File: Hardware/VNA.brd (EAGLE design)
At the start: 122 x 96 mm, 502 parts, among them IC1 MIC2253, IC10 MAX2871, IC11 RFSW6042, IC12 RFSW6042, IC13 QPC6324, IC14 RFSA3714, IC15 TRF37A73, IC16 QPC6324, IC17 QPC6324, IC18 QPC6324, IC19 AP2114H, IC2 LM3370SD-4221, IC20 NCP702-3.3, IC21 MAX2871, IC22 LT5560, IC23 THS4521IDGKR, IC24 ADL5801, IC25 NCP702-1.8, IC26 MCP33131D-10-E/MS, IC27 LT5560, IC28 THS4521IDGKR, IC29 ADL5801, IC3 LDL212PU50R, IC30 NCP702-1.8, IC31 MCP33131D-10-E/MS, IC32 THS4521IDGKR, IC33 ADL5801, IC34 NCP702-1.8, IC35 MCP33131D-10-E/MS, IC36 LT5560, IC37 STM32G431CB, IC4 LDL212PU50R, IC5 LDL212PU50R, IC6 LDL212PU50R, IC7 SI5351C, IC8 AP2114H, IC9 NCP702-3.3, J1 DNP, J2 AMPHENOL_132289, J3 AMPHENOL_132289, J4 TYPE-C16P(073), Q1 DSB221SDN/26MHz, T1 B012-617DB-1-63-B331, T2 B012-617DB-1-63-B331, T3 B012-617DB-1-63-B331, U1 W25Q16BVSN, U2 6SLX9TQG144, X1 SMA_CONNECTOR, X2 SMA_CONNECTOR, X3 DNP

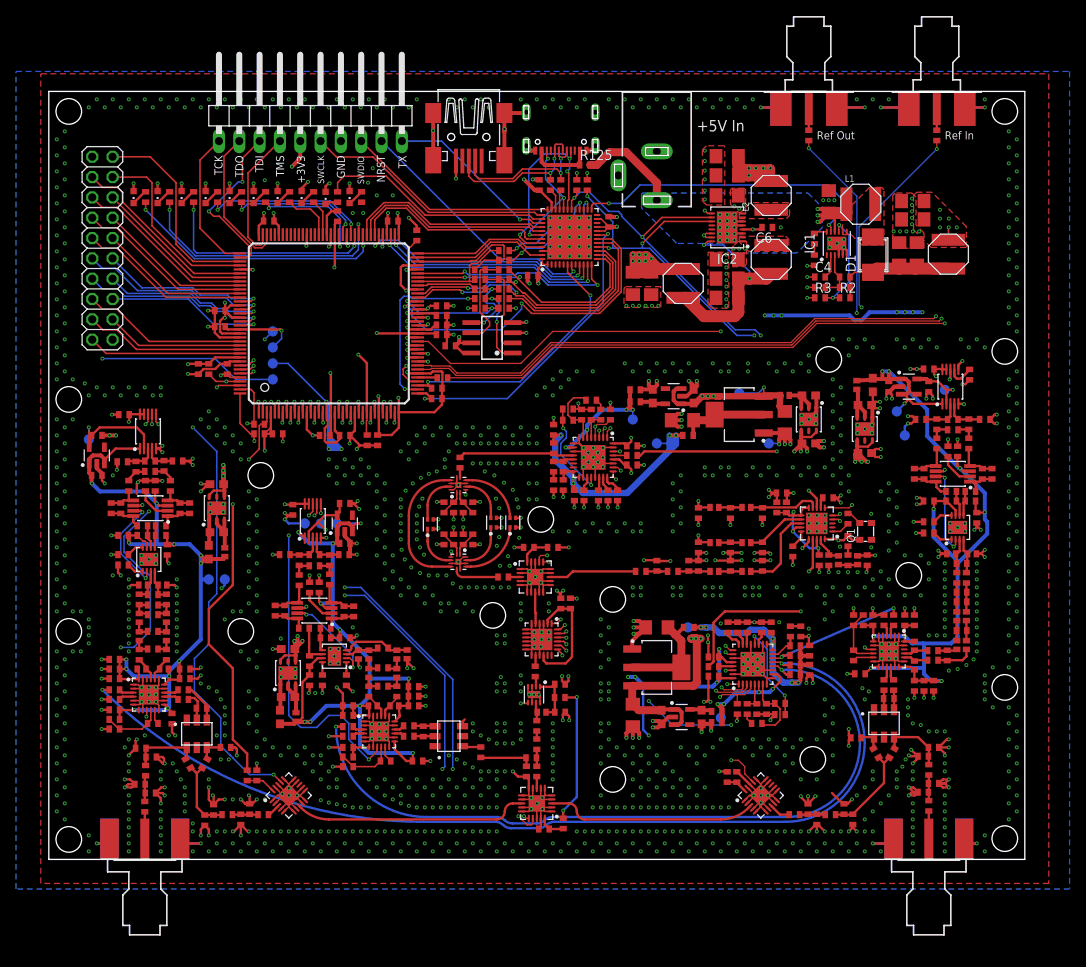
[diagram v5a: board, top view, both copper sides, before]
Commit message: Additional screws
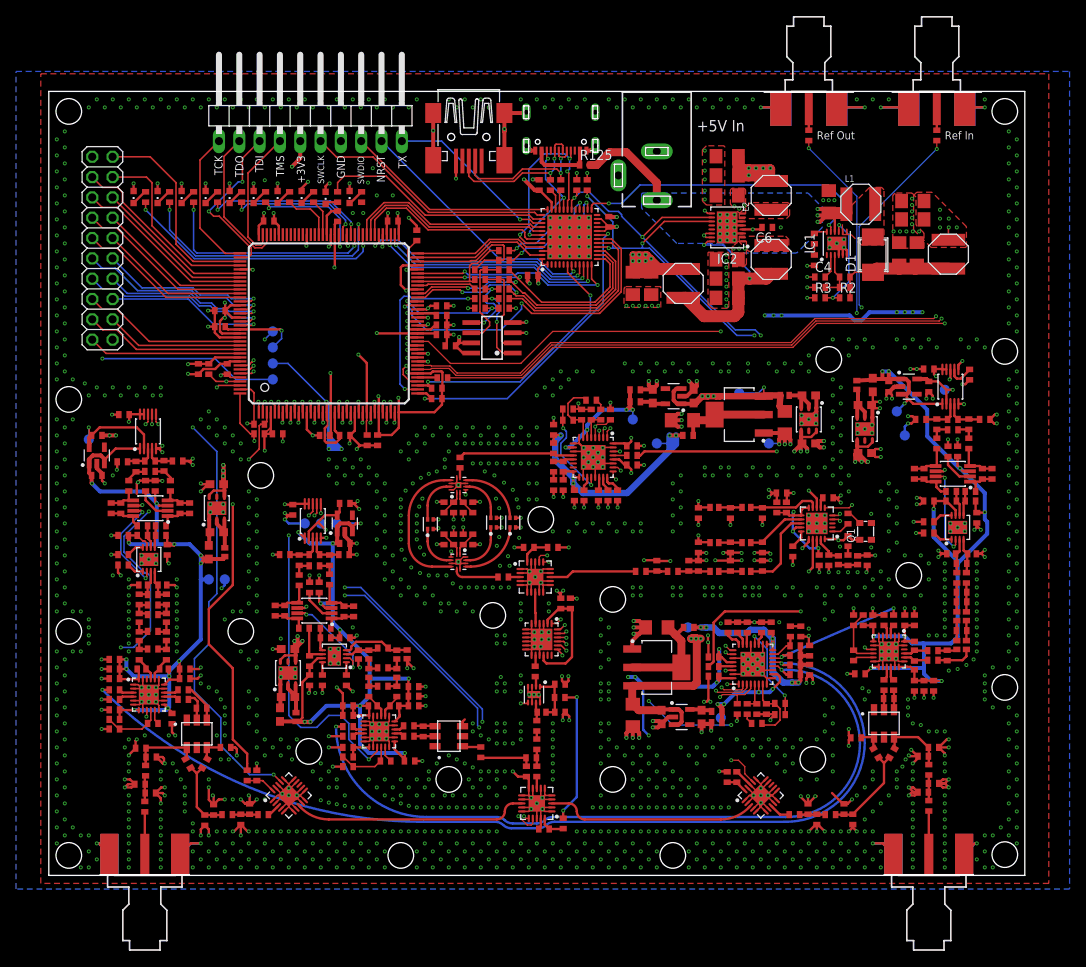
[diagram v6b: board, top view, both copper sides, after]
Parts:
- moved J2 1.90 mm to (12.0, -1.90)
- moved J3 1.90 mm to (110.0, -1.90)
- moved C175 1.00 mm to (45.1, 12.3)
- moved C28 0.30 mm to (28.9, 18.1)
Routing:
- net PORTSWITCH2: track 71.5 -> 69.2 mm
- net PORTSWITCH1: track 70.6 -> 68.3 mm
- net GND: track 729.2 -> 731.5 mm, vias 1584 -> 1681
- net +5V/3: track 106.3 -> 104.3 mm
- net N$6: track 3.38 -> 5.28 mm
- net N$239: track 3.48 -> 5.38 mm
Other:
- board size 122 x 96 mm -> 122 x 98 mm

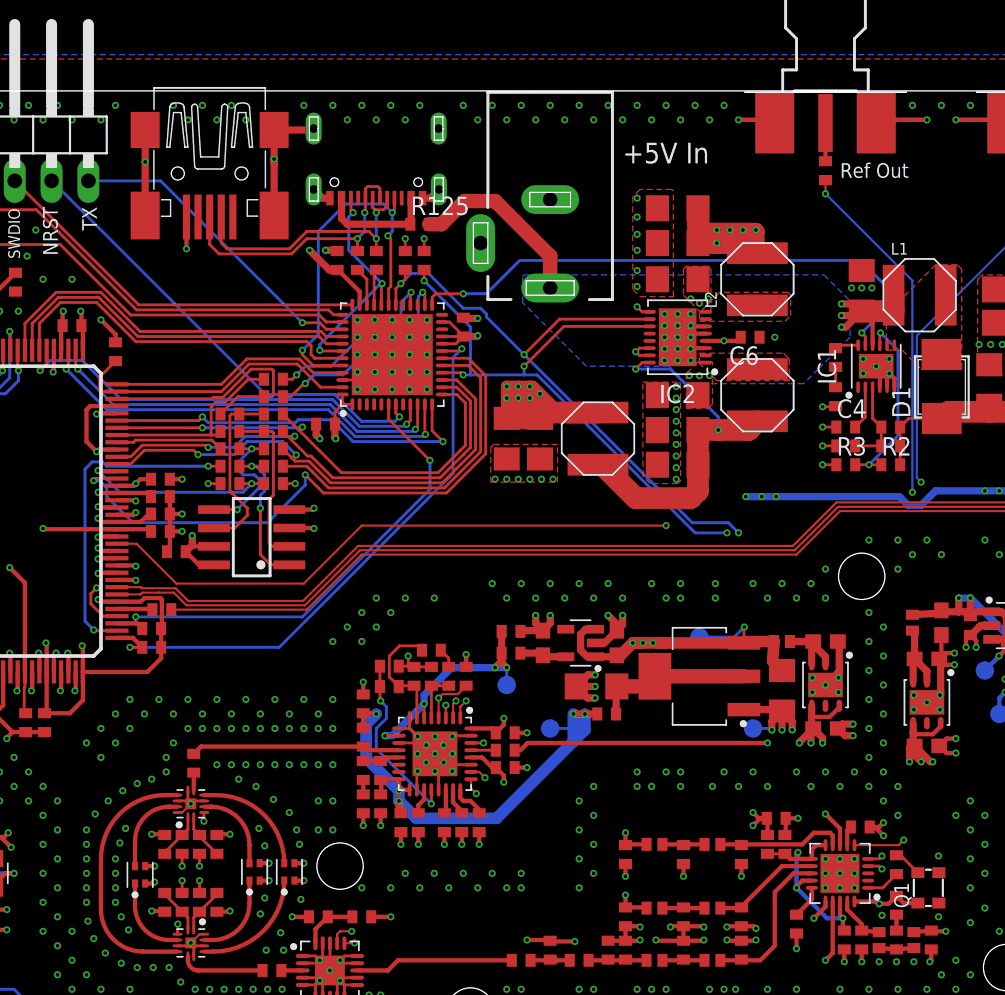
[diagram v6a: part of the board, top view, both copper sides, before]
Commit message: DC jack with power priority over USB
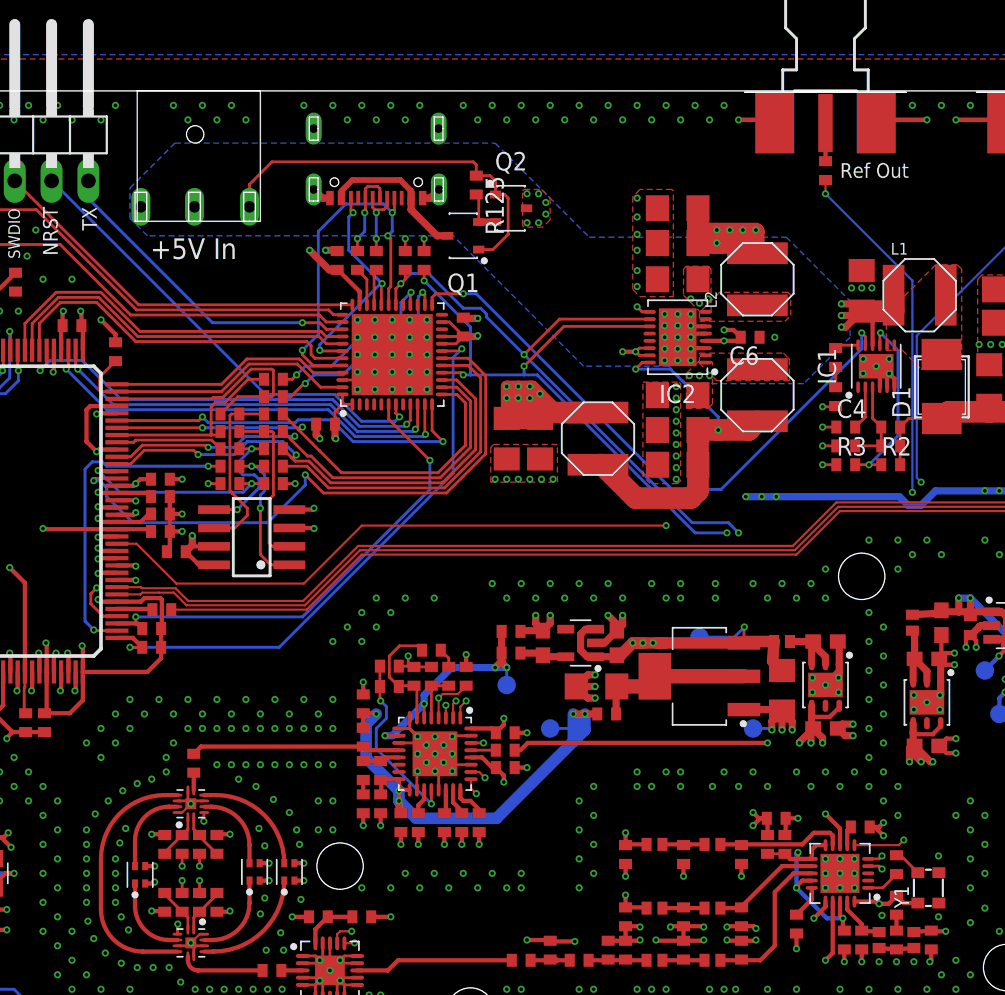
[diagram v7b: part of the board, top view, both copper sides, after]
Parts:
- removed X3: DNP, VNA:32005-301
- added Q2: SSM3J338R, VNA:SOTFL95P240X80-3N
- added Y1: DSB221SDN/26MHz, crystal-geyer_V1_0:2.5X2.0_KXO-86-TCXO
- J1: value DNP -> PJ-014D; device VNA:DCJ0202 -> VNA:PJ-014D
- Q1: value DSB221SDN/26MHz -> SSM3J338R; device crystal-geyer_V1_0:2.5X2.0_KXO-86-TCXO -> VNA:SOTFL95P240X80-3N
- R125: value 0 -> 10k
- moved Q1 55.3 mm to (70.0, 86.0), turned to 180 degrees
- moved J1 22.6 mm to (56.0, 96.0)
- moved R125 4.74 mm to (70.9, 89.5), turned to 270 degrees
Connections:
- removed net N$185: J4.11, J4.2, R125.1
- new net N$167: Q1.2, Q2.2, R125.2
- new net N$168: J1.3, Q1.1, Q2.1, R125.1
- new net USB_POWER: J4.11, J4.2, Q1.3
- net +3V3: now also Y1.4; no longer Q1.4
- net +5V: now also Q2.3; no longer R125.2
- net GND: now also J1.2, Y1.1, Y1.2; no longer J1.3, Q1.1, Q1.2, X3.5, X3.M1, X3.M2, X3.M3, X3.M4
- net N$113: now also Y1.3; no longer Q1.3
- net N$186: no longer X3.3
- net N$189: no longer X3.2
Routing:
- net N$168: track 0.00 -> 27.0 mm
- net GND: track 731.5 -> 714.6 mm, vias 1681 -> 1678
- net N$189: track 18.6 -> 5.26 mm
- net N$186: track 19.1 -> 6.30 mm
- net +5V: track 28.4 -> 17.9 mm, vias 11 -> 19
- net USB_POWER: track 0.00 -> 10.5 mm
- net N$185: track 8.22 -> 0.00 mm
- net EN_6V: track 38.4 -> 41.9 mm
- net N$167: track 0.00 -> 3.13 mm
- net UART_TX: track 21.8 -> 22.5 mm

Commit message: Updated BOM
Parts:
- L6, L7, L8, L9: device VNA:L0402 -> VNA:R0402
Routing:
- net GND: vias 1678 -> 1683
